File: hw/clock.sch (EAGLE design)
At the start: 46 parts, among them IC1 AT90S2313S, IC2 PCF2123TSSOP14, Q1 BSS84, Q2 BSS84, Q3 BSS84, Q4 BSS84, U1 TLC59282_DBQ_24, X1 4MHz, X2 CRYSTALTFORK_SMD

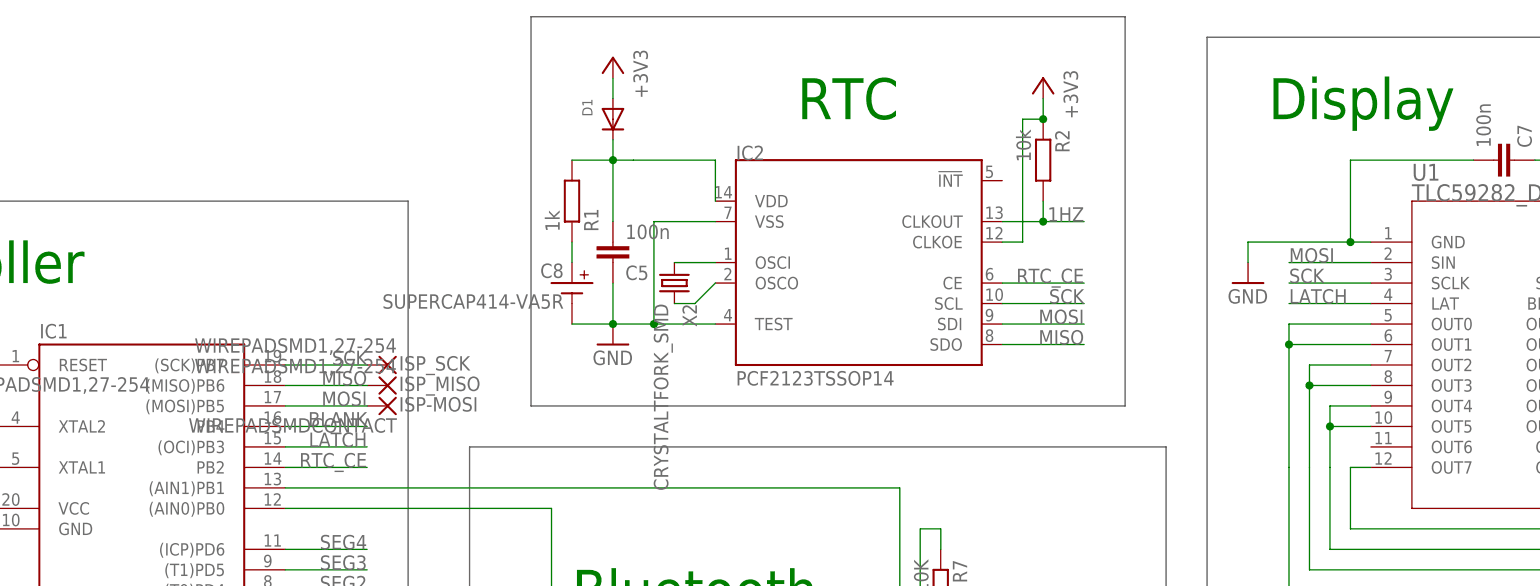
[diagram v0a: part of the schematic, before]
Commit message: Fix reversed SPI lines, remove superfluous pull-up on RTC.CLKOUT, improve vias.
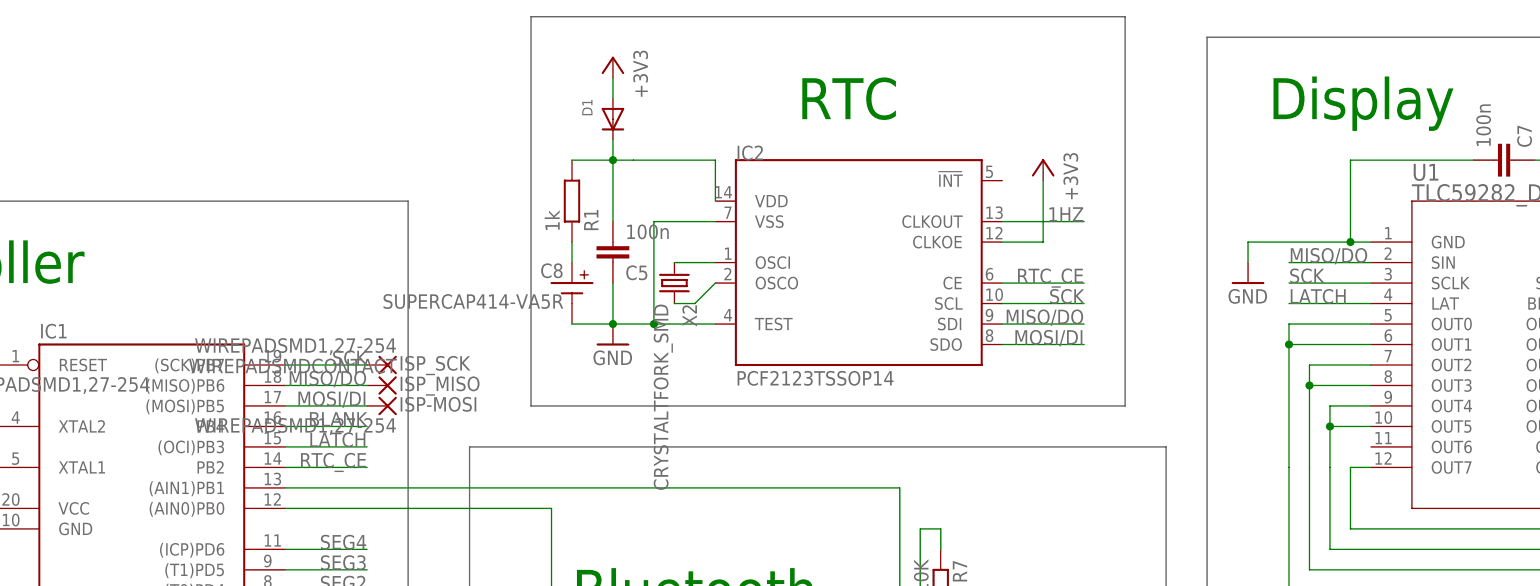
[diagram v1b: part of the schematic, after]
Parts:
- removed R2: 10k, rcl:R-EU_R0603
- ISP-MOSI: value WIREPADSMDCONTACT -> WIREPADSMD1,27-254; device jocki:WIREPADSMDCONTACT -> jocki:WIREPADSMD1,27-254
- ISP_MISO: value WIREPADSMD1,27-254 -> WIREPADSMDCONTACT; device jocki:WIREPADSMD1,27-254 -> jocki:WIREPADSMDCONTACT
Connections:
- removed net MISO: IC1.(MISO)PB6, IC2.SDO, ISP_MISO.P
- removed net MOSI: IC1.(MOSI)PB5, IC2.SDI, ISP-MOSI.P, U1.SIN
- new net MISO/DO: IC1.(MISO)PB6, IC2.SDI, ISP_MISO.P, U1.SIN
- new net MOSI/DI: IC1.(MOSI)PB5, IC2.SDO, ISP-MOSI.P
- net +3V3: no longer R2.1
- net 1HZ: no longer R2.2

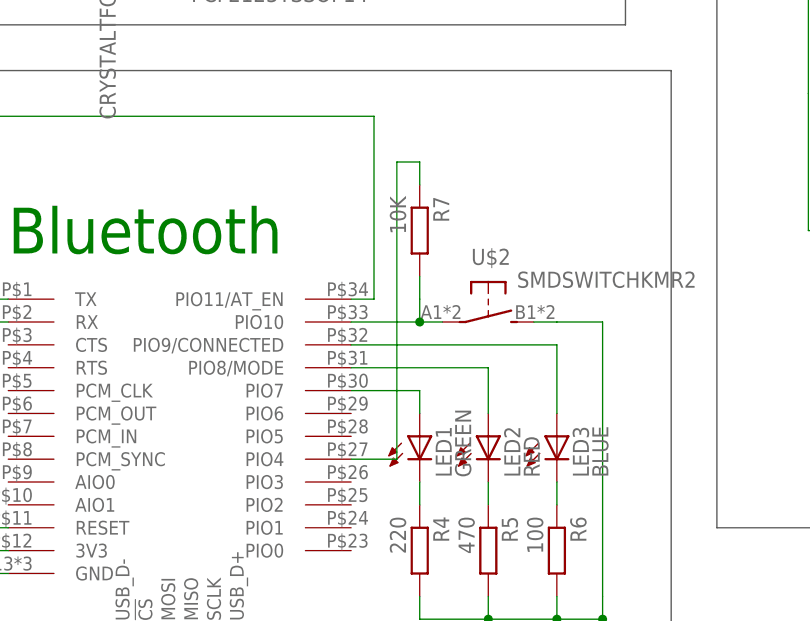
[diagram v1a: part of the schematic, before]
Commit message: Connect button to BT module's AT_ENABLE pin
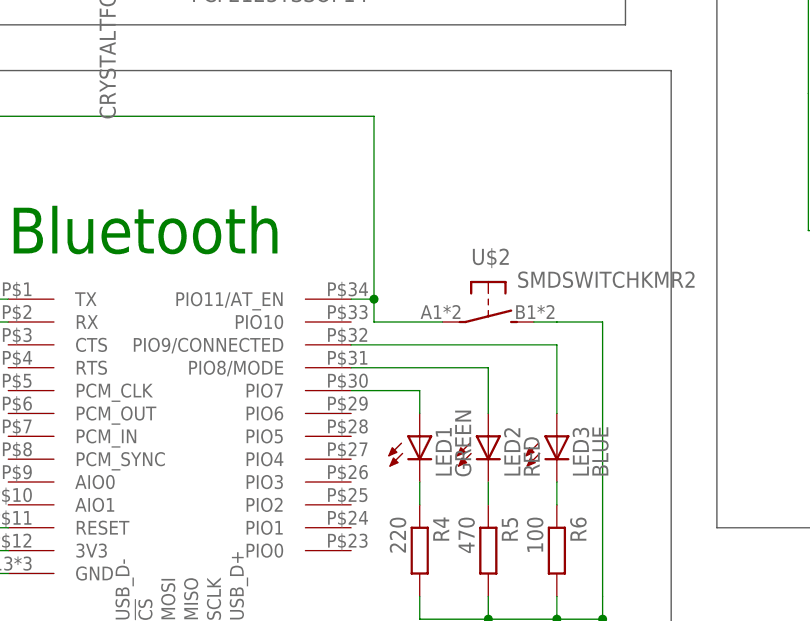
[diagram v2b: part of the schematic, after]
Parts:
- removed R7: 10K, rcl:R-EU_R0603
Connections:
- removed net N$11: R7.2, U$1.PIO10, U$2.P
- removed net N$20: R7.1, U$1.PIO4
- net N$8: now also U$2.P
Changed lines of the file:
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@@
 <grid distance="0.1" unitdist="inch" unit="inch" style="lines" multiple="1" display="no" altdistance="0.01" altunitdist="inch" altunit="inch"/>
 <layers>
-<layer number="1" name="Top" color="4" fill="1" visible="yes" active="no"/>
-<layer number="16" name="Bottom" color="1" fill="1" visible="yes" active="no"/>
-<layer number="17" name="Pads" color="2" fill="1" visible="yes" active="no"/>
-<layer number="18" name="Vias" color="2" fill="1" visible="yes" active="no"/>
-<layer number="19" name="Unrouted" color="6" fill="1" visible="yes" active="no"/>
-<layer number="20" name="Dimension" color="15" fill="1" visible="yes" active="no"/>
-<layer number="21" name="tPlace" color="7" fill="1" visible="yes" active="no"/>
-<layer number="22" name="bPlace" color="7" fill="1" visible="yes" active="no"/>
-<layer number="23" name="tOrigins" color="15" fill="1" visible="yes" active="no"/>
-<layer number="24" name="bOrigins" color="15" fill="1" visible="yes" active="no"/>
-<layer number="25" name="tNames" color="7" fill="1" visible="yes" active="no"/>
-<layer number="26" name="bNames" color="7" fill="1" visible="yes" active="no"/>
-<layer number="27" name="tValues" color="7" fill="1" visible="yes" active="no"/>
-<layer number="28" name="bValues" color="7" fill="1" visible="yes" active="no"/>
+<layer number="1" name="Top" color="4" fill="1" visible="no" active="no"/>
+<layer number="16" name="Bottom" color="1" fill="1" visible="no" active="no"/>
+<layer number="17" name="Pads" color="2" fill="1" visible="no" active="no"/>
+<layer number="18" name="Vias" color="2" fill="1" visible="no" active="no"/>
+<layer number="19" name="Unrouted" color="6" fill="1" visible="no" active="no"/>
+<layer number="20" name="Dimension" color="15" fill="1" visible="no" active="no"/>
+<layer number="21" name="tPlace" color="7" fill="1" visible="no" active="no"/>
+<layer number="22" name="bPlace" color="7" fill="1" visible="no" active="no"/>
+<layer number="23" name="tOrigins" color="15" fill="1" visible="no" active="no"/>
+<layer number="24" name="bOrigins" color="15" fill="1" visible="no" active="no"/>
+<layer number="25" name="tNames" color="7" fill="1" visible="no" active="no"/>
+<layer number="26" name="bNames" color="7" fill="1" visible="no" active="no"/>
+<layer number="27" name="tValues" color="7" fill="1" visible="no" active="no"/>
+<layer number="28" name="bValues" color="7" fill="1" visible="no" active="no"/>
 <layer number="29" name="tStop" color="7" fill="3" visible="no" active="no"/>
 <layer number="30" name="bStop" color="7" fill="6" visible="no" active="no"/>
@@
 <layer number="35" name="tGlue" color="7" fill="4" visible="no" active="no"/>
 <layer number="36" name="bGlue" color="7" fill="5" visible="no" active="no"/>
-<layer number="37" name="tTest" color="7" fill="1" visible="yes" active="no"/>
-<layer number="38" name="bTest" color="7" fill="1" visible="yes" active="no"/>
+<layer number="37" name="tTest" color="7" fill="1" visible="no" active="no"/>
+<layer number="38" name="bTest" color="7" fill="1" visible="no" active="no"/>
 <layer number="39" name="tKeepout" color="4" fill="11" visible="no" active="no"/>
 <layer number="40" name="bKeepout" color="1" fill="11" visible="no" active="no"/>
@@
 <layer number="44" name="Drills" color="7" fill="1" visible="no" active="no"/>
 <layer number="45" name="Holes" color="7" fill="1" visible="no" active="no"/>
-<layer number="46" name="Milling" color="3" fill="1" visible="yes" active="no"/>
-<layer number="47" name="Measures" color="7" fill="1" visible="yes" active="no"/>
-<layer number="48" name="Document" color="7" fill="1" visible="yes" active="no"/>
-<layer number="49" name="Reference" color="7" fill="1" visible="yes" active="no"/>
-<layer number="50" name="dxf" color="7" fill="1" visible="yes" active="no"/>
-<layer number="51" name="tDocu" color="7" fill="1" visible="yes" active="no"/>
-<layer number="52" name="bDocu" color="7" fill="1" visible="yes" active="no"/>
-<layer number="53" name="tGND_GNDA" color="7" fill="9" visible="yes" active="no"/>
-<layer number="54" name="bGND_GNDA" color="1" fill="9" visible="yes" active="no"/>
-<layer number="56" name="wert" color="7" fill="1" visible="yes" active="no"/>
+<layer number="46" name="Milling" color="3" fill="1" visible="no" active="no"/>
+<layer number="47" name="Measures" color="7" fill="1" visible="no" active="no"/>
+<layer number="48" name="Document" color="7" fill="1" visible="no" active="no"/>
+<layer number="49" name="Reference" color="7" fill="1" visible="no" active="no"/>
+<layer number="50" name="dxf" color="7" fill="1" visible="no" active="no"/>
+<layer number="51" name="tDocu" color="7" fill="1" visible="no" active="no"/>
+<layer number="52" name="bDocu" color="7" fill="1" visible="no" active="no"/>
+<layer number="53" name="tGND_GNDA" color="7" fill="9" visible="no" active="no"/>
+<layer number="54" name="bGND_GNDA" color="1" fill="9" visible="no" active="no"/>
+<layer number="56" name="wert" color="7" fill="1" visible="no" active="no"/>
 <layer number="91" name="Nets" color="2" fill="1" visible="yes" active="yes"/>
 <layer number="92" name="Busses" color="1" fill="1" visible="yes" active="yes"/>
@@
 <part name="R5" library="rcl" deviceset="R-EU_" device="R0603" value="470"/>
 <part name="R6" library="rcl" deviceset="R-EU_" device="R0603" value="100"/>
-<part name="R7" library="rcl" deviceset="R-EU_" device="R0603" value="10K"/>
 <part name="GND9" library="supply1" deviceset="GND" device=""/>
 <part name="C6" library="rcl" deviceset="C-EU" device="C0603K" value="100n"/>
@@
 <instance part="R5" gate="G$1" x="152.4" y="38.1" rot="R270"/>
 <instance part="R6" gate="G$1" x="160.02" y="38.1" rot="R270"/>
-<instance part="R7" gate="G$1" x="144.78" y="73.66" rot="R270"/>
 <instance part="GND9" gate="1" x="165.1" y="25.4"/>
 <instance part="C6" gate="G$1" x="17.78" y="81.28" rot="R90"/>
@@
 <pinref part="IC1" gate="G$1" pin="(AIN1)PB1"/>
 <wire x1="63.5" y1="86.36" x2="139.7" y2="86.36" width="0.1524" layer="91"/>
+<pinref part="U$2" gate="G$1" pin="P"/>
+<wire x1="147.32" y1="63.5" x2="139.7" y2="63.5" width="0.1524" layer="91"/>
+<wire x1="139.7" y1="63.5" x2="139.7" y2="66.04" width="0.1524" layer="91"/>
+<junction x="139.7" y="66.04"/>
 </segment>
 </net>
@@
 </segment>
 </net>
-<net name="N$11" class="0">
-<segment>
-<wire x1="144.78" y1="66.04" x2="144.78" y2="63.5" width="0.1524" layer="91"/>
-<pinref part="U$1" gate="G$1" pin="PIO10"/>
-<wire x1="144.78" y1="63.5" x2="137.16" y2="63.5" width="0.1524" layer="91"/>
-<wire x1="144.78" y1="63.5" x2="147.32" y2="63.5" width="0.1524" layer="91"/>
-<pinref part="R7" gate="G$1" pin="2"/>
-<wire x1="144.78" y1="66.04" x2="144.78" y2="68.58" width="0.1524" layer="91"/>
-<junction x="144.78" y="63.5"/>
-<pinref part="U$2" gate="G$1" pin="P"/>
-</segment>
-</net>
 <net name="N$13" class="0">
 <segment>
@@
 </segment>
 </net>
-<net name="N$20" class="0">
-<segment>
-<pinref part="R7" gate="G$1" pin="1"/>
-<wire x1="144.78" y1="78.74" x2="144.78" y2="81.28" width="0.1524" layer="91"/>
-<wire x1="144.78" y1="81.28" x2="142.24" y2="81.28" width="0.1524" layer="91"/>
-<wire x1="142.24" y1="81.28" x2="142.24" y2="48.26" width="0.1524" layer="91"/>
-<pinref part="U$1" gate="G$1" pin="PIO4"/>
-<wire x1="142.24" y1="48.26" x2="137.16" y2="48.26" width="0.1524" layer="91"/>
-</segment>
-</net>

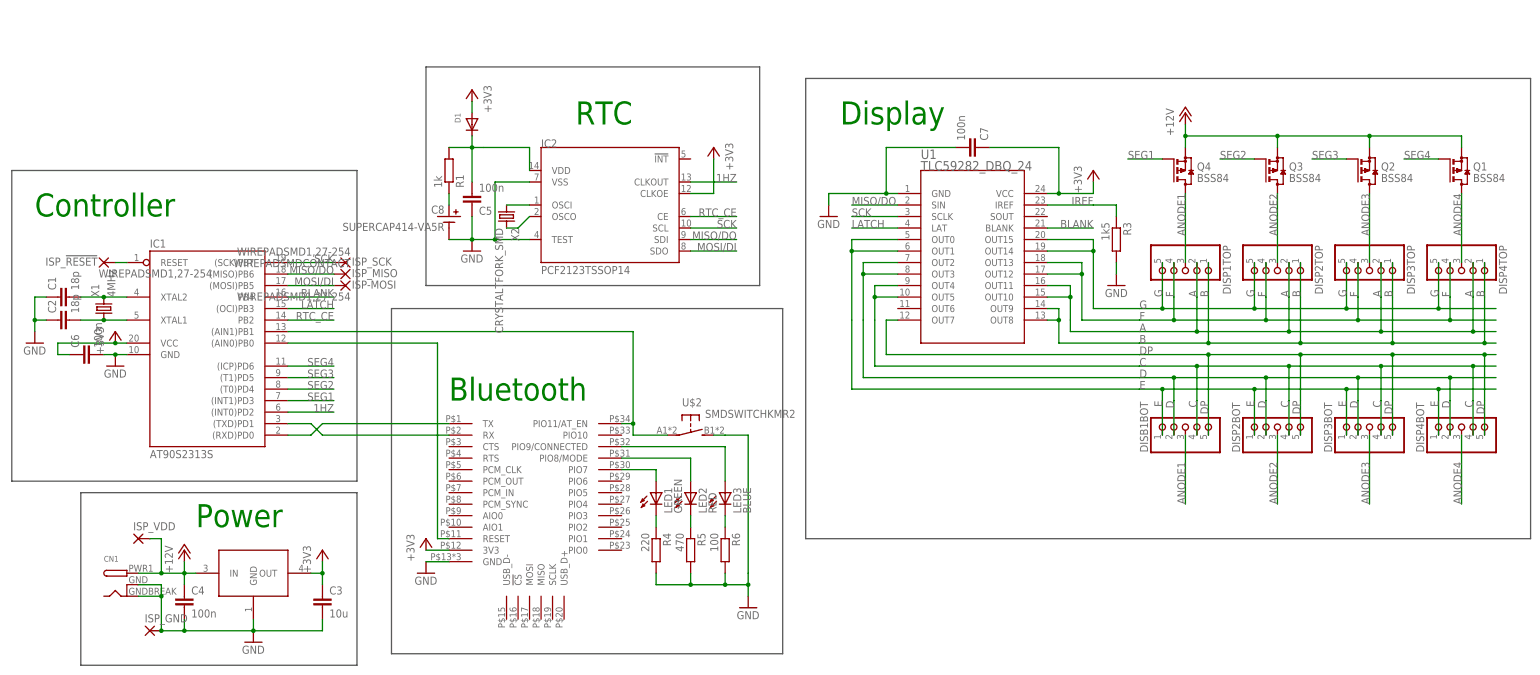
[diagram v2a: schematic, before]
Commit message: HW v2.0, with proper level shifters
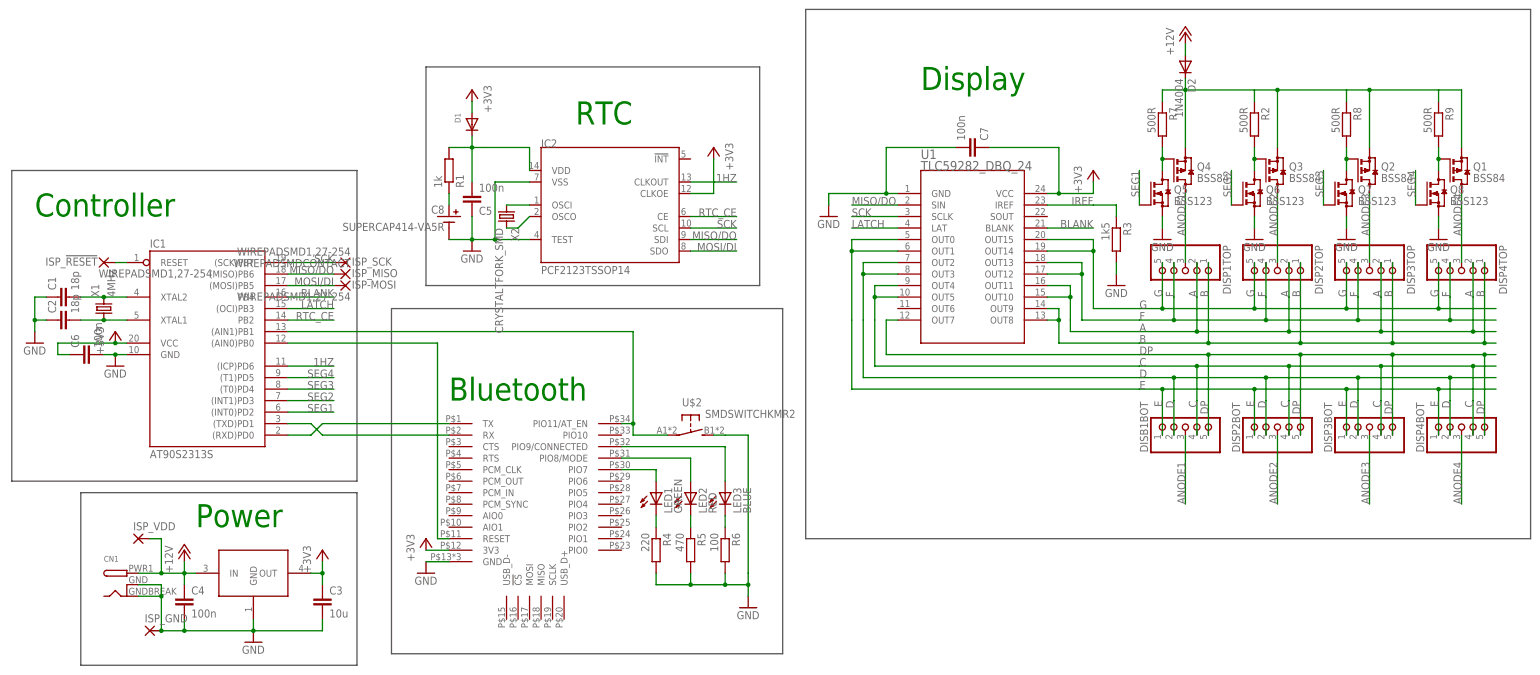
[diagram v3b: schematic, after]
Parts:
- added D2: 1N4004, adafruit:1N4004
- added Q5, Q6, Q7, Q8: BSS123, transistor-small-signal:BSS123
- added R2, R7, R8, R9: 500R, rcl:R-EU_R0603
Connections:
- new net N$11: D2.C, Q1.S, Q2.S, Q3.S, Q4.S, R2.1, R7.1, R8.1, R9.1
- new net N$28: Q1.G, Q8.D, R9.2
- new net N$29: Q2.G, Q7.D, R8.2
- new net N$30: Q3.G, Q6.D, R2.2
- new net N$31: Q4.G, Q5.D, R7.2
- net +12V: now also D2.A; no longer Q1.S, Q2.S, Q3.S, Q4.S
- net 1HZ: now also IC1.(ICP)PD6; no longer IC1.(INT0)PD2
- net GND: now also Q5.S, Q6.S, Q7.S, Q8.S
- net SEG1: now also IC1.(INT0)PD2, Q5.G; no longer IC1.(INT1)PD3, Q4.G
- net SEG2: now also IC1.(INT1)PD3, Q6.G; no longer IC1.(T0)PD4, Q3.G
- net SEG3: now also IC1.(T0)PD4, Q7.G; no longer IC1.(T1)PD5, Q2.G
- net SEG4: now also IC1.(T1)PD5, Q8.G; no longer IC1.(ICP)PD6, Q1.G
